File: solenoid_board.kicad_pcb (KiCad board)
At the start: 2 copper layers, 170 x 145 mm, 34 parts, among them J2 MCU_LEFT_LEGS, J3 MCU_RIGHT_LEGS

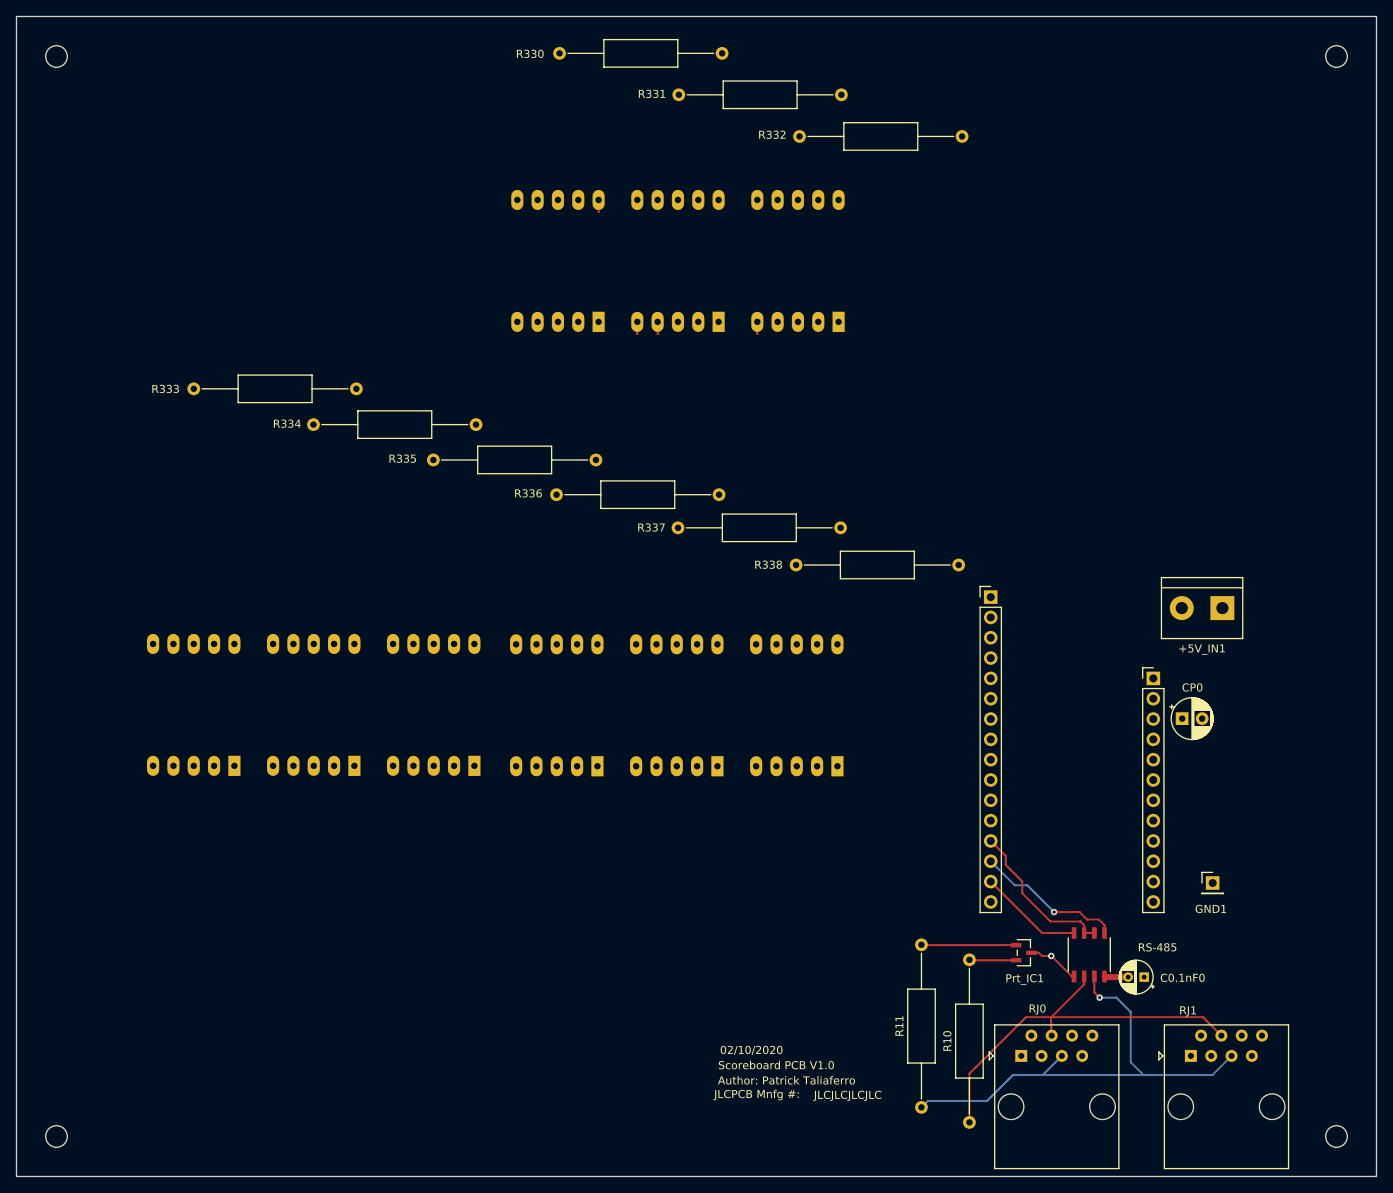
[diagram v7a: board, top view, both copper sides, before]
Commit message: Major revisions occurred to the Schematic. Sourced 7-Segment display and MosFETs.
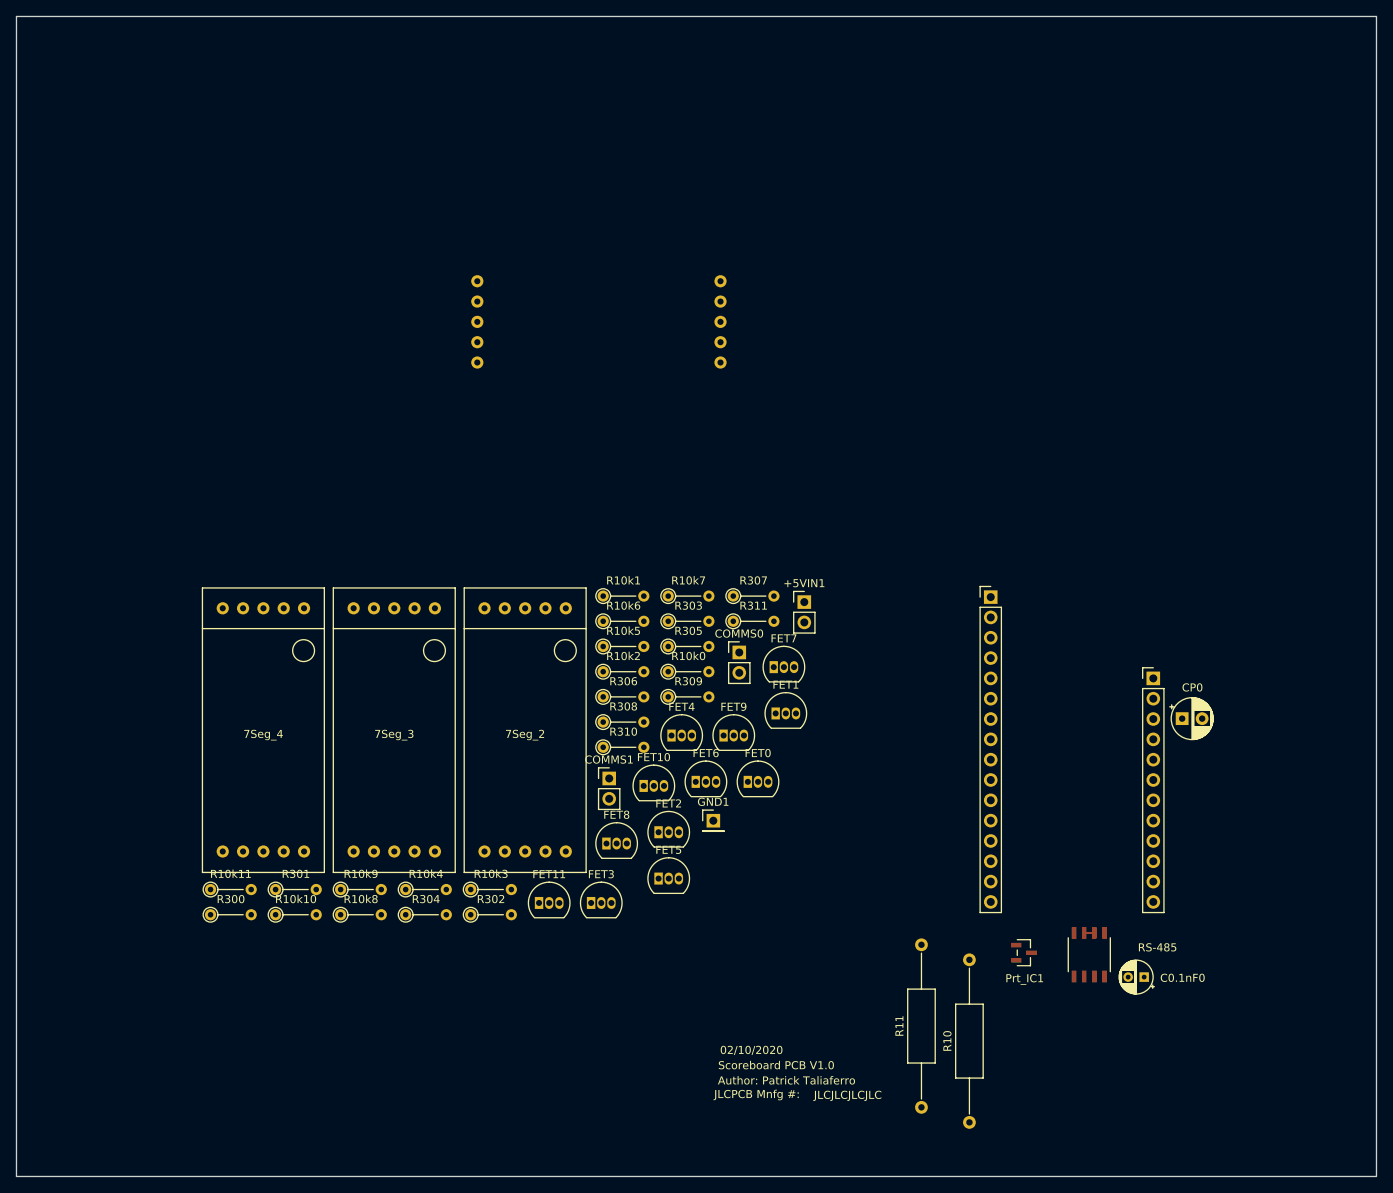
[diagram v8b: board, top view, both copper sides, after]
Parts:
- removed +5V_IN1: MCU_PWR_Supply, TerminalBlock:TerminalBlock_bornier-2_P5.08mm
- removed 7Seg_5, 7Seg_6, 7Seg_7, 7Seg_8, 7Seg_9: Conn_02x05_Top_Bottom, Display_7Segment:7SegmentLED_LTS6760_LTS6780
- removed R330, R331, R332: 330, Resistor_THT:R_Axial_DIN0309_L9.0mm_D3.2mm_P20.32mm_Horizontal
- removed R333, R334, R335, R336, R337, R338: R, Resistor_THT:R_Axial_DIN0309_L9.0mm_D3.2mm_P20.32mm_Horizontal
- removed REF** (x4): MountingHole_2.7mm_M2.5, MountingHole:MountingHole_2.7mm_M2.5
- removed RJ0, RJ1: RJ45, Connector_RJ:RJ45_Amphenol_54602-x08_Horizontal
- added +5VIN1: Conn_01x02, Connector_PinHeader_2.54mm:PinHeader_1x02_P2.54mm_Vertical, F.Cu at (153.5, 88.2)
- added COMMS0: Conn_01x02, Connector_PinHeader_2.54mm:PinHeader_1x02_P2.54mm_Vertical, F.Cu at (145.3, 94.5)
- added COMMS1: Conn_01x02, Connector_PinHeader_2.54mm:PinHeader_1x02_P2.54mm_Vertical, F.Cu at (129.1, 110.3)
- added FET0: 2N7000, Package_TO_SOT_THT:TO-92_Inline, F.Cu at (146.4, 110.7)
- added FET1: 2N7000, Package_TO_SOT_THT:TO-92_Inline, F.Cu at (149.9, 102.1)
- added FET10: 2N7000, Package_TO_SOT_THT:TO-92_Inline, F.Cu at (133.4, 111.2)
- added FET11: 2N7000, Package_TO_SOT_THT:TO-92_Inline, F.Cu at (120.3, 125.8)
- added FET2: 2N7000, Package_TO_SOT_THT:TO-92_Inline, F.Cu at (135.3, 117.0)
- added FET3: 2N7000, Package_TO_SOT_THT:TO-92_Inline, F.Cu at (126.8, 125.8)
- added FET4: 2N7000, Package_TO_SOT_THT:TO-92_Inline, F.Cu at (136.9, 104.9)
- added FET5: 2N7000, Package_TO_SOT_THT:TO-92_Inline, F.Cu at (135.3, 122.8)
- added FET6: 2N7000, Package_TO_SOT_THT:TO-92_Inline, F.Cu at (139.9, 110.7)
- added FET7: 2N7000, Package_TO_SOT_THT:TO-92_Inline, F.Cu at (149.7, 96.3)
- added FET8: 2N7000, Package_TO_SOT_THT:TO-92_Inline, F.Cu at (128.7, 118.4)
- added FET9: 2N7000, Package_TO_SOT_THT:TO-92_Inline, F.Cu at (143.4, 104.9)
- added R10k0: 10k, Resistor_THT:R_Axial_DIN0204_L3.6mm_D1.6mm_P5.08mm_Vertical, F.Cu at (136.5, 96.9)
- added R10k1: 10k, Resistor_THT:R_Axial_DIN0204_L3.6mm_D1.6mm_P5.08mm_Vertical, F.Cu at (128.3, 87.5)
- added R10k10: 10k, Resistor_THT:R_Axial_DIN0204_L3.6mm_D1.6mm_P5.08mm_Vertical, F.Cu at (87.4, 127.3)
- added R10k11: 10k, Resistor_THT:R_Axial_DIN0204_L3.6mm_D1.6mm_P5.08mm_Vertical, F.Cu at (79.3, 124.1)
- added R10k2: 10k, Resistor_THT:R_Axial_DIN0204_L3.6mm_D1.6mm_P5.08mm_Vertical, F.Cu at (128.3, 96.9)
- added R10k3: 10k, Resistor_THT:R_Axial_DIN0204_L3.6mm_D1.6mm_P5.08mm_Vertical, F.Cu at (111.8, 124.1)
- added R10k4: 10k, Resistor_THT:R_Axial_DIN0204_L3.6mm_D1.6mm_P5.08mm_Vertical, F.Cu at (103.6, 124.1)
- added R10k5: 10k, Resistor_THT:R_Axial_DIN0204_L3.6mm_D1.6mm_P5.08mm_Vertical, F.Cu at (128.3, 93.8)
- added R10k6: 10k, Resistor_THT:R_Axial_DIN0204_L3.6mm_D1.6mm_P5.08mm_Vertical, F.Cu at (128.3, 90.6)
- added R10k7: 10k, Resistor_THT:R_Axial_DIN0204_L3.6mm_D1.6mm_P5.08mm_Vertical, F.Cu at (136.5, 87.5)
- added R10k8: 10k, Resistor_THT:R_Axial_DIN0204_L3.6mm_D1.6mm_P5.08mm_Vertical, F.Cu at (95.5, 127.3)
- added R10k9: 10k, Resistor_THT:R_Axial_DIN0204_L3.6mm_D1.6mm_P5.08mm_Vertical, F.Cu at (95.5, 124.1)
- added R300: 300, Resistor_THT:R_Axial_DIN0204_L3.6mm_D1.6mm_P5.08mm_Vertical, F.Cu at (79.3, 127.3)
- added R301: 300, Resistor_THT:R_Axial_DIN0204_L3.6mm_D1.6mm_P5.08mm_Vertical, F.Cu at (87.4, 124.1)
- added R302: 300, Resistor_THT:R_Axial_DIN0204_L3.6mm_D1.6mm_P5.08mm_Vertical, F.Cu at (111.8, 127.3)
- added R303: 300, Resistor_THT:R_Axial_DIN0204_L3.6mm_D1.6mm_P5.08mm_Vertical, F.Cu at (136.5, 90.6)
- added R304: 300, Resistor_THT:R_Axial_DIN0204_L3.6mm_D1.6mm_P5.08mm_Vertical, F.Cu at (103.6, 127.3)
- added R305: 300, Resistor_THT:R_Axial_DIN0204_L3.6mm_D1.6mm_P5.08mm_Vertical, F.Cu at (136.5, 93.8)
- added R306: 300, Resistor_THT:R_Axial_DIN0204_L3.6mm_D1.6mm_P5.08mm_Vertical, F.Cu at (128.3, 100.1)
- added R307: 300, Resistor_THT:R_Axial_DIN0204_L3.6mm_D1.6mm_P5.08mm_Vertical, F.Cu at (144.6, 87.5)
- added R308: 300, Resistor_THT:R_Axial_DIN0204_L3.6mm_D1.6mm_P5.08mm_Vertical, F.Cu at (128.3, 103.2)
- added R309: 300, Resistor_THT:R_Axial_DIN0204_L3.6mm_D1.6mm_P5.08mm_Vertical, F.Cu at (136.5, 100.1)
- added R310: 300, Resistor_THT:R_Axial_DIN0204_L3.6mm_D1.6mm_P5.08mm_Vertical, F.Cu at (128.3, 106.4)
- added R311: 300, Resistor_THT:R_Axial_DIN0204_L3.6mm_D1.6mm_P5.08mm_Vertical, F.Cu at (144.6, 90.6)
- 7Seg_1: footprint Display_7Segment:7SegmentLED_LTS6760_LTS6780 -> Kingbright_10-DinDisplay:SC10-21SRWA
- 7Seg_2, 7Seg_3, 7Seg_4: footprint Display_7Segment:7SegmentLED_LTS6760_LTS6780 -> Kingbright_10-DinDisplay:SC10-21SRWA; moved to F.Cu
- GND1: value Conn_01x01_Male -> Conn_01x01
- moved 7Seg_3 75.4 mm to (102.2, 104.2), turned to 0 degrees
- moved GND1 62.9 mm to (142.1, 115.5)
- moved 7Seg_2 56.5 mm to (118.6, 104.2), turned to 0 degrees
- moved 7Seg_4 5.75 mm to (85.9, 104.2), turned to 0 degrees
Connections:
- net /RJ45_5 renamed /B
- 7Seg_1 pad 1: /A4 -> /e
- 7Seg_1 pad 10: /A0 -> /g
- 7Seg_1 pad 2: /A5 -> /d
- 7Seg_1 pad 4: /C -> /c
- 7Seg_1 pad 5: /DP -> /dp
- 7Seg_1 pad 6: /A3 -> /b
- 7Seg_1 pad 7: /A -> /a
- 7Seg_1 pad 9: /A1 -> /f
- 7Seg_2 pad 1: /A4 -> /e
- 7Seg_2 pad 10: /A0 -> /g
- 7Seg_2 pad 2: /A5 -> /d
- 7Seg_2 pad 4: /C -> /c
- 7Seg_2 pad 5: /DP -> /dp
- 7Seg_2 pad 6: /A3 -> /b
- 7Seg_2 pad 7: /A -> /a
- 7Seg_2 pad 9: /A1 -> /f
- 7Seg_3 pad 1: /A4 -> /e
- 7Seg_3 pad 10: /A0 -> /g
- 7Seg_3 pad 2: /A5 -> /d
- 7Seg_3 pad 4: /C -> /c
- 7Seg_3 pad 5: /DP -> /dp
- 7Seg_3 pad 6: /A3 -> /b
- 7Seg_3 pad 7: /A -> /a
- 7Seg_3 pad 8: /Third_Display -> (no net)
- 7Seg_3 pad 9: /A1 -> /f
- 7Seg_4 pad 1: /A4 -> /e
- 7Seg_4 pad 10: /A0 -> /g
- 7Seg_4 pad 2: /A5 -> /d
- 7Seg_4 pad 4: /C -> /c
- 7Seg_4 pad 5: /DP -> /dp
- 7Seg_4 pad 6: /A3 -> /b
- 7Seg_4 pad 7: /A -> /a
- 7Seg_4 pad 9: /A1 -> /f
- J2 pad 11: /C -> /SCK
- J2 pad 12: /DP -> /MOSI
- J2 pad 7: /A -> /A2
- J2 pad 9: /A4 -> (no net)
- J3 pad 10: /D5 -> (no net)
- J3 pad 11: /SCL -> (no net)
- J3 pad 12: /SDA -> (no net)
- J3 pad 8: /D9 -> (no net)
- J3 pad 9: /D6 -> (no net)
- R10 pad 1: /RJ45_4 -> /A
- RS-485 pad 6: /RJ45_4 -> /A
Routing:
- net /B: track 61.8 -> 0.00 mm, vias 1 -> 0
- net /RJ45_4: track 50.9 -> 0.00 mm
- net /MISO: track 19.8 -> 1.27 mm
- net /RX0: track 18.5 -> 0.00 mm, vias 1 -> 0
- net /TX1: track 13.1 -> 0.00 mm
- net Net-(Prt_IC1-Pad1): track 11.9 -> 0.00 mm
- net GND: track 6.55 -> 0.00 mm, vias 1 -> 0
- net Net-(Prt_IC1-Pad2): track 5.88 -> 0.00 mm
- net /DP: track 3.08 -> 0.00 mm
- net +3V3: track 2.98 -> 0.00 mm
- net /C: track 1.56 -> 0.00 mm
- net /A0: track 1.52 -> 0.00 mm
